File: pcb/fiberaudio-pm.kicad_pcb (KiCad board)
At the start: 2 copper layers, 25.4 x 22.9 mm, 9 parts, among them J1 Conn_01x06, J2 PLT237/T10WH, J3 PLR237/T10BK

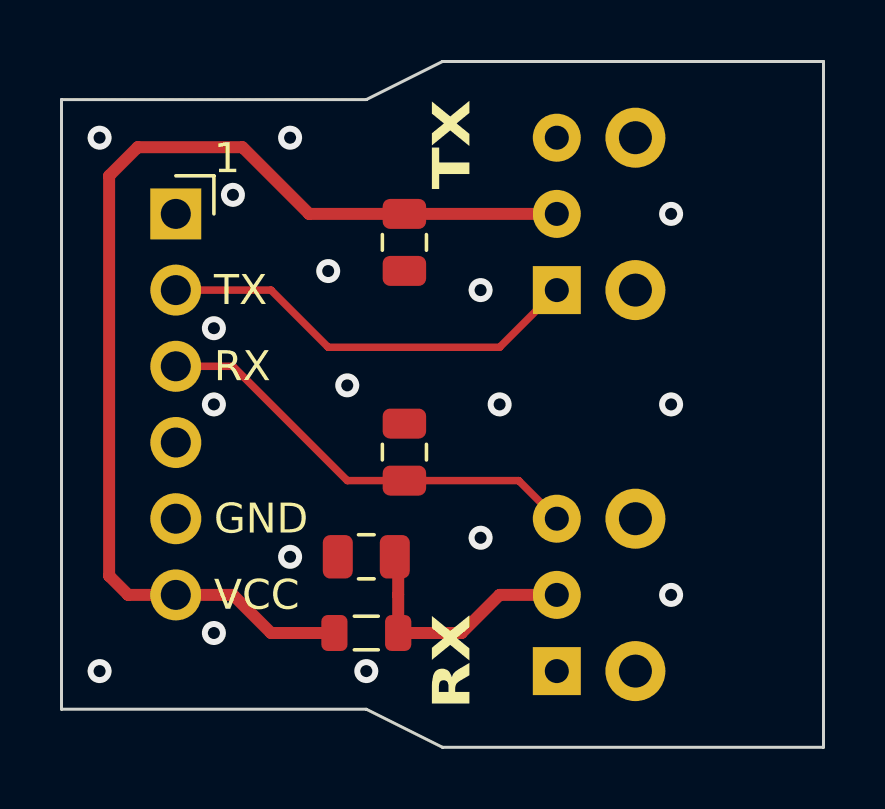
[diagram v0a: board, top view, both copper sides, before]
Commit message: Fixed pin-swap on J3; Updated to Rev.2; Updated documentation
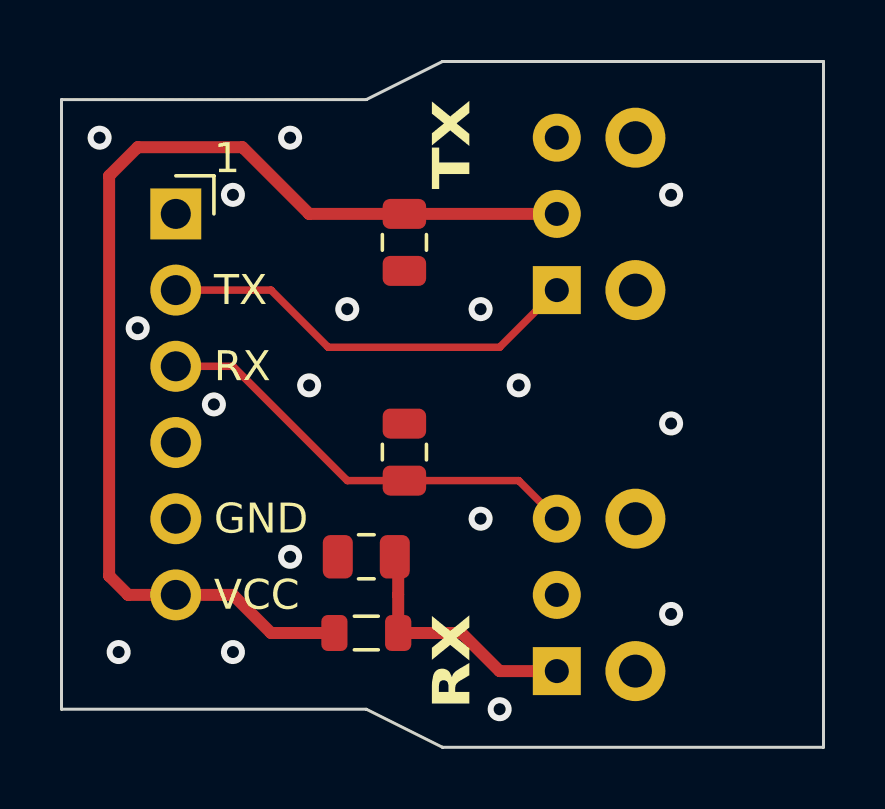
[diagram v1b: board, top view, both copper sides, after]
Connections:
- C31 pad 1: Net-(J3-VCC) -> Net-(J3-GND)
- J3 pad 1: GND -> Net-(J3-GND)
- J3 pad 2: Net-(J3-VCC) -> GND
- L31 pad 2: Net-(J3-VCC) -> Net-(J3-GND)
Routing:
- net Net-(J3-VCC): track 8.40 -> 0.00 mm
- net Net-(J3-GND): track 0.00 -> 8.40 mm
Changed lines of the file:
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@@
     (title "fiberaudio-pm")
     (date "2024-01-22")
-    (rev "1")
+    (rev "2")
     (company "https://github.com/islandcontroller/fiberaudio-pm")
   )
@@
   (net 0 "")
   (net 1 "GND")
-  (net 2 "Net-(J3-VCC)")
+  (net 2 "Net-(J3-GND)")
   (net 3 "/RX")
   (net 4 "unconnected-(J1-Pin_1-Pad1)")
@@
       (stroke (width 0.1) (type solid)) (layer "F.Fab"))
     (pad "1" smd roundrect (at -0.95 0 180) (size 1 1.45) (layers "F.Cu" "F.Paste" "F.Mask") (roundrect_rratio 0.25)
-      (net 2 "Net-(J3-VCC)") (pintype "passive"))
+      (net 2 "Net-(J3-GND)") (pintype "passive"))
     (pad "2" smd roundrect (at 0.95 0 180) (size 1 1.45) (layers "F.Cu" "F.Paste" "F.Mask") (roundrect_rratio 0.25)
       (net 1 "GND") (pintype "passive"))
@@
       (stroke (width 0.12) (type solid)) (layer "F.Fab"))
     (pad "1" thru_hole rect (at -2.54 0 90) (size 1.6 1.6) (drill 0.8) (layers "*.Cu" "*.Mask")
+      (net 2 "Net-(J3-GND)") (pinfunction "VCC") (pintype "power_in"))
+    (pad "2" thru_hole circle (at 0 0 90) (size 1.6 1.6) (drill 0.8) (layers "*.Cu" "*.Mask")
       (net 1 "GND") (pinfunction "GND") (pintype "power_in"))
-    (pad "2" thru_hole circle (at 0 0 90) (size 1.6 1.6) (drill 0.8) (layers "*.Cu" "*.Mask")
-      (net 2 "Net-(J3-VCC)") (pinfunction "VCC") (pintype "power_in"))
     (pad "3" thru_hole circle (at 2.54 0 90) (size 1.6 1.6) (drill 0.8) (layers "*.Cu" "*.Mask")
       (net 3 "/RX") (pinfunction "OUT") (pintype "output"))
@@
       (net 7 "VCC") (pinfunction "1") (pintype "passive"))
     (pad "2" smd roundrect (at 1.0625 0) (size 0.875 1.2) (layers "F.Cu" "F.Paste" "F.Mask") (roundrect_rratio 0.25)
-      (net 2 "Net-(J3-VCC)") (pinfunction "2") (pintype "passive"))
+      (net 2 "Net-(J3-GND)") (pinfunction "2") (pintype "passive"))
     (model "${KICAD6_3DMODEL_DIR}/Inductor_SMD.3dshapes/L_0805_2012Metric.wrl"
       (offset (xyz 0 0 0))
@@
     (effects (font (size 1.25 1.5) (thickness 0.25) bold) (justify right))
   )
-  (via (at 99.695 60.325) (size 0.8) (drill 0.4) (layers "F.Cu" "B.Cu") (free) (net 1))
+  (via (at 98.425 60.325) (size 0.8) (drill 0.4) (layers "F.Cu" "B.Cu") (free) (net 1))
   (via (at 97.79 66.04) (size 0.8) (drill 0.4) (layers "F.Cu" "B.Cu") (free) (net 1))
-  (via (at 104.775 60.96) (size 0.8) (drill 0.4) (layers "F.Cu" "B.Cu") (free) (net 1))
+  (via (at 105.41 60.325) (size 0.8) (drill 0.4) (layers "F.Cu" "B.Cu") (free) (net 1))
   (via (at 95.885 53.975) (size 0.8) (drill 0.4) (layers "F.Cu" "B.Cu") (free) (net 1))
-  (via (at 91.44 69.85) (size 0.8) (drill 0.4) (layers "F.Cu" "B.Cu") (free) (net 1))
-  (via (at 100.33 69.85) (size 0.8) (drill 0.4) (layers "F.Cu" "B.Cu") (free) (net 1))
-  (via (at 104.14 57.15) (size 0.8) (drill 0.4) (layers "F.Cu" "B.Cu") (free) (net 1))
-  (via (at 95.25 58.42) (size 0.8) (drill 0.4) (layers "F.Cu" "B.Cu") (free) (net 1))
-  (via (at 95.25 68.58) (size 0.8) (drill 0.4) (layers "F.Cu" "B.Cu") (free) (net 1))
-  (via (at 110.49 54.61) (size 0.8) (drill 0.4) (layers "F.Cu" "B.Cu") (free) (net 1))
-  (via (at 99.06 56.515) (size 0.8) (drill 0.4) (layers "F.Cu" "B.Cu") (free) (net 1))
-  (via (at 110.49 60.96) (size 0.8) (drill 0.4) (layers "F.Cu" "B.Cu") (free) (net 1))
-  (via (at 110.49 67.31) (size 0.8) (drill 0.4) (layers "F.Cu" "B.Cu") (free) (net 1))
-  (via (at 104.14 65.405) (size 0.8) (drill 0.4) (layers "F.Cu" "B.Cu") (free) (net 1))
+  (via (at 104.14 64.77) (size 0.8) (drill 0.4) (layers "F.Cu" "B.Cu") (free) (net 1))
+  (via (at 92.075 69.215) (size 0.8) (drill 0.4) (layers "F.Cu" "B.Cu") (free) (net 1))
+  (via (at 104.775 71.12) (size 0.8) (drill 0.4) (layers "F.Cu" "B.Cu") (free) (net 1))
+  (via (at 104.14 57.785) (size 0.8) (drill 0.4) (layers "F.Cu" "B.Cu") (free) (net 1))
+  (via (at 92.71 58.42) (size 0.8) (drill 0.4) (layers "F.Cu" "B.Cu") (free) (net 1))
+  (via (at 95.885 69.215) (size 0.8) (drill 0.4) (layers "F.Cu" "B.Cu") (free) (net 1))
+  (via (at 110.49 53.975) (size 0.8) (drill 0.4) (layers "F.Cu" "B.Cu") (free) (net 1))
+  (via (at 99.695 57.785) (size 0.8) (drill 0.4) (layers "F.Cu" "B.Cu") (free) (net 1))
+  (via (at 110.49 61.595) (size 0.8) (drill 0.4) (layers "F.Cu" "B.Cu") (free) (net 1))
+  (via (at 110.49 67.945) (size 0.8) (drill 0.4) (layers "F.Cu" "B.Cu") (free) (net 1))
   (via (at 95.25 60.96) (size 0.8) (drill 0.4) (layers "F.Cu" "B.Cu") (free) (net 1))
   (via (at 97.79 52.07) (size 0.8) (drill 0.4) (layers "F.Cu" "B.Cu") (free) (net 1))
   (via (at 91.44 52.07) (size 0.8) (drill 0.4) (layers "F.Cu" "B.Cu") (free) (net 1))
-  (segment (start 103.505 68.58) (end 101.3925 68.58) (width 0.4) (layer "F.Cu") (net 2))
-  (segment (start 106.68 67.31) (end 104.775 67.31) (width 0.4) (layer "F.Cu") (net 2))
-  (segment (start 104.775 67.31) (end 103.505 68.58) (width 0.4) (layer "F.Cu") (net 2))
+  (segment (start 101.3925 68.58) (end 103.505 68.58) (width 0.4) (layer "F.Cu") (net 2))
+  (segment (start 104.775 69.85) (end 106.68 69.85) (width 0.4) (layer "F.Cu") (net 2))
+  (segment (start 103.505 68.58) (end 104.775 69.85) (width 0.4) (layer "F.Cu") (net 2))
   (segment (start 101.3925 68.58) (end 101.3925 67.31) (width 0.4) (layer "F.Cu") (net 2))
   (segment (start 101.3925 66.1525) (end 101.28 66.04) (width 0.4) (layer "F.Cu") (net 2))

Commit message: Re-classified as 'component' acc. to FAQ on Directive 2012/19/EU (WEEE2), see http://ec.europa.eu/environment/waste/weee/pdf/faq.pdf; Removed WEEE logo; Added note regarding RoHS compliance requirement
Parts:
- removed the REF** at (100.3, 54.6)
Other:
- board text added: "Subject to compliance with RoHS Directive (EU) 2015/863 amending Annex II to Directive 2011/65/EU."

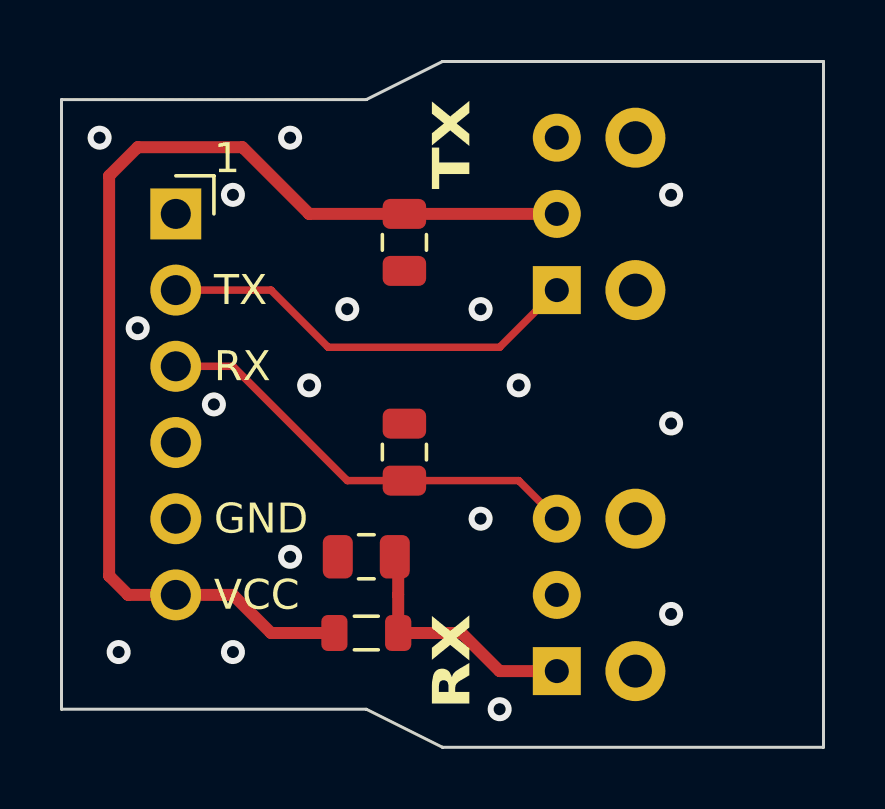
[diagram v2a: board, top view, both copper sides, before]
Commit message: Reduced thermal spoke width to 0.25um; Adjusted layout; Adjusted text placement and size
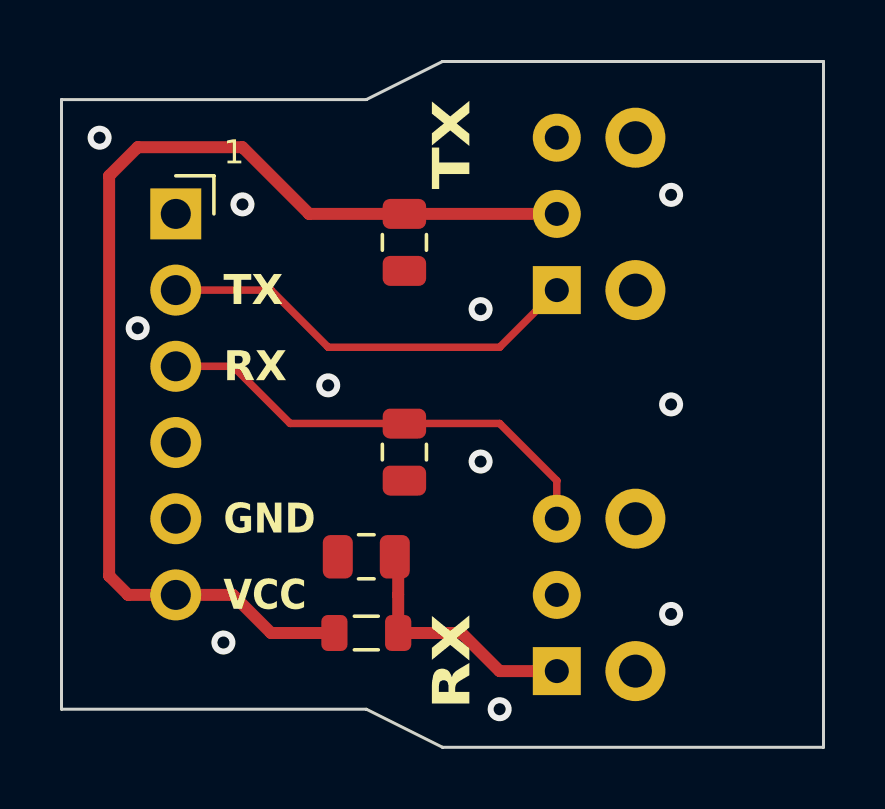
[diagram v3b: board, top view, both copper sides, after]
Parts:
- turned C32 to -90 degrees
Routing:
- net /RX: track 14.8 -> 15.5 mm
- net GND: vias 17 -> 11
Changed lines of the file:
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@@
   (title_block
     (title "fiberaudio-pm")
-    (date "2024-01-25")
-    (rev "3")
+    (date "2024-01-26")
+    (rev "4")
     (company "https://github.com/islandcontroller/fiberaudio-pm")
   )
@@
   (net 11 "unconnected-(J3-NC-Pad5)")
   (footprint "Capacitor_SMD:C_0805_2012Metric" (layer "F.Cu")
-    (at 101.6 62.55 90)
+    (at 101.6 62.55 -90)
     (descr "Capacitor SMD 0805 (2012 Metric), square (rectangular) end terminal, IPC_7351 nominal, (Body size source: IPC-SM-782 page 76, https://www.pcb-3d.com/wordpress/wp-content/uploads/ipc-sm-782a_amendment_1_and_2.pdf, https://docs.google.com/spreadsheets/d/1BsfQQcO9C6DZCsRaXUlFlo91Tg2WpOkGARC1WS5S8t0/edit?usp=sharing), generated with kicad-footprint-generator")
     (tags "capacitor")
@@
     (fp_line (start 1 0.625) (end -1 0.625)
       (stroke (width 0.1) (type solid)) (layer "F.Fab"))
-    (pad "1" smd roundrect (at -0.95 0 90) (size 1 1.45) (layers "F.Cu" "F.Paste" "F.Mask") (roundrect_rratio 0.25)
+    (pad "1" smd roundrect (at -0.95 0 270) (size 1 1.45) (layers "F.Cu" "F.Paste" "F.Mask") (roundrect_rratio 0.25)
       (net 3 "/RX") (pintype "passive"))
-    (pad "2" smd roundrect (at 0.95 0 90) (size 1 1.45) (layers "F.Cu" "F.Paste" "F.Mask") (roundrect_rratio 0.25)
+    (pad "2" smd roundrect (at 0.95 0 270) (size 1 1.45) (layers "F.Cu" "F.Paste" "F.Mask") (roundrect_rratio 0.25)
       (net 1 "GND") (pintype "passive"))
     (model "${KICAD6_3DMODEL_DIR}/Capacitor_SMD.3dshapes/C_0805_2012Metric.wrl"
@@
     (pad "4" thru_hole oval (at 0 7.62) (size 1.7 1.7) (drill 1) (layers "*.Cu" "*.Mask")
       (net 6 "unconnected-(J1-Pin_4-Pad4)") (pinfunction "Pin_4") (pintype "passive+no_connect"))
-    (pad "5" thru_hole oval (at 0 10.16) (size 1.7 1.7) (drill 1) (layers "*.Cu" "*.Mask")
+    (pad "5" thru_hole oval (at 0 10.16 45) (size 1.7 1.7) (drill 1) (layers "*.Cu" "*.Mask")
       (net 1 "GND") (pinfunction "Pin_5") (pintype "passive"))
     (pad "6" thru_hole oval (at 0 12.7) (size 1.7 1.7) (drill 1) (layers "*.Cu" "*.Mask")
@@
     (effects (font (size 1.25 1.5) (thickness 0.25) bold) (justify left))
   )
-  (gr_text "TX" (at 95.25 57.15) (layer "F.SilkS")
-    (effects (font (size 1 1) (thickness 0.15)) (justify left))
-  )
-  (gr_text "GND" (at 95.25 64.77) (layer "F.SilkS")
-    (effects (font (size 1 1) (thickness 0.15)) (justify left))
-  )
-  (gr_text "1" (at 95.25 53.34) (layer "F.SilkS")
-    (effects (font (size 1 1) (thickness 0.15)) (justify left bottom))
-  )
-  (gr_text "RX" (at 95.25 59.69) (layer "F.SilkS")
-    (effects (font (size 1 1) (thickness 0.15)) (justify left))
-  )
-  (gr_text "VCC" (at 95.25 67.31) (layer "F.SilkS")
-    (effects (font (size 1 1) (thickness 0.15)) (justify left))
+  (gr_text "TX" (at 95.5675 57.15) (layer "F.SilkS")
+    (effects (font (size 1 1) (thickness 0.2) bold) (justify left))
+  )
+  (gr_text "GND" (at 95.5675 64.77) (layer "F.SilkS")
+    (effects (font (size 1 0.9) (thickness 0.2) bold) (justify left))
+  )
+  (gr_text "1" (at 95.5675 53.0225) (layer "F.SilkS")
+    (effects (font (size 0.8 0.8) (thickness 0.15)) (justify left bottom))
+  )
+  (gr_text "RX" (at 95.5675 59.69) (layer "F.SilkS")
+    (effects (font (size 1 1) (thickness 0.2) bold) (justify left))
+  )
+  (gr_text "VCC" (at 95.5675 67.31) (layer "F.SilkS")
+    (effects (font (size 1 0.9) (thickness 0.2) bold) (justify left))
   )
   (gr_text "TX" (at 103.1875 50.8 90) (layer "F.SilkS")
@@
     (effects (font (size 1 1) (thickness 0.15)) (justify left top))
   )
-  (via (at 98.425 60.325) (size 0.8) (drill 0.4) (layers "F.Cu" "B.Cu") (free) (net 1))
-  (via (at 97.79 66.04) (size 0.8) (drill 0.4) (layers "F.Cu" "B.Cu") (free) (net 1))
-  (via (at 105.41 60.325) (size 0.8) (drill 0.4) (layers "F.Cu" "B.Cu") (free) (net 1))
-  (via (at 95.885 53.975) (size 0.8) (drill 0.4) (layers "F.Cu" "B.Cu") (free) (net 1))
-  (via (at 104.14 64.77) (size 0.8) (drill 0.4) (layers "F.Cu" "B.Cu") (free) (net 1))
-  (via (at 92.075 69.215) (size 0.8) (drill 0.4) (layers "F.Cu" "B.Cu") (free) (net 1))
+  (via (at 96.2025 54.2925) (size 0.8) (drill 0.4) (layers "F.Cu" "B.Cu") (free) (net 1))
+  (via (at 104.14 62.865) (size 0.8) (drill 0.4) (layers "F.Cu" "B.Cu") (free) (net 1))
+  (via (at 95.5675 68.8975) (size 0.8) (drill 0.4) (layers "F.Cu" "B.Cu") (free) (net 1))
   (via (at 104.775 71.12) (size 0.8) (drill 0.4) (layers "F.Cu" "B.Cu") (free) (net 1))
   (via (at 104.14 57.785) (size 0.8) (drill 0.4) (layers "F.Cu" "B.Cu") (free) (net 1))
   (via (at 92.71 58.42) (size 0.8) (drill 0.4) (layers "F.Cu" "B.Cu") (free) (net 1))
-  (via (at 95.885 69.215) (size 0.8) (drill 0.4) (layers "F.Cu" "B.Cu") (free) (net 1))
   (via (at 110.49 53.975) (size 0.8) (drill 0.4) (layers "F.Cu" "B.Cu") (free) (net 1))
-  (via (at 99.695 57.785) (size 0.8) (drill 0.4) (layers "F.Cu" "B.Cu") (free) (net 1))
-  (via (at 110.49 61.595) (size 0.8) (drill 0.4) (layers "F.Cu" "B.Cu") (free) (net 1))
+  (via (at 110.49 60.96) (size 0.8) (drill 0.4) (layers "F.Cu" "B.Cu") (free) (net 1))
   (via (at 110.49 67.945) (size 0.8) (drill 0.4) (layers "F.Cu" "B.Cu") (free) (net 1))
-  (via (at 95.25 60.96) (size 0.8) (drill 0.4) (layers "F.Cu" "B.Cu") (free) (net 1))
-  (via (at 97.79 52.07) (size 0.8) (drill 0.4) (layers "F.Cu" "B.Cu") (free) (net 1))
+  (via (at 99.06 60.325) (size 0.8) (drill 0.4) (layers "F.Cu" "B.Cu") (free) (net 1))
   (via (at 91.44 52.07) (size 0.8) (drill 0.4) (layers "F.Cu" "B.Cu") (free) (net 1))
   (segment (start 101.3925 68.58) (end 103.505 68.58) (width 0.4) (layer "F.Cu") (net 2))
@@
   (segment (start 101.3925 66.1525) (end 101.28 66.04) (width 0.4) (layer "F.Cu") (net 2))
   (segment (start 101.3925 67.31) (end 101.3925 66.1525) (width 0.4) (layer "F.Cu") (net 2))
-  (segment (start 99.695 63.5) (end 101.6 63.5) (width 0.25) (layer "F.Cu") (net 3))
-  (segment (start 105.41 63.5) (end 106.68 64.77) (width 0.25) (layer "F.Cu") (net 3))
-  (segment (start 95.885 59.69) (end 99.695 63.5) (width 0.25) (layer "F.Cu") (net 3))
-  (segment (start 101.6 63.5) (end 105.41 63.5) (width 0.25) (layer "F.Cu") (net 3))
+  (segment (start 104.775 61.595) (end 106.68 63.5) (width 0.25) (layer "F.Cu") (net 3))
+  (segment (start 106.68 63.5) (end 106.68 64.77) (width 0.25) (layer "F.Cu") (net 3))
+  (segment (start 97.79 61.595) (end 104.775 61.595) (width 0.25) (layer "F.Cu") (net 3))
   (segment (start 93.98 59.69) (end 95.885 59.69) (width 0.25) (layer "F.Cu") (net 3))
+  (segment (start 95.885 59.69) (end 97.79 61.595) (width 0.25) (layer "F.Cu") (net 3))
   (segment (start 93.98 57.15) (end 97.155 57.15) (width 0.25) (layer "F.Cu") (net 5))
   (segment (start 99.06 59.055) (end 104.775 59.055) (width 0.25) (layer "F.Cu") (net 5))
@@
     (polygon
       (pts
-        (xy 99.232867 67.705525)
-        (xy 101.307686 67.721862)
-        (xy 101.307686 69.40459)
-        (xy 99.200192 69.388253)
+        (xy 99.06 67.945)
+        (xy 101.307686 67.945)
+        (xy 101.307686 69.215)
+        (xy 99.06 69.215)
       )
     )
@@
     (connect_pads (clearance 0.25))
     (min_thickness 0.25) (filled_areas_thickness no)
-    (fill yes (thermal_gap 0.25) (thermal_bridge_width 0.508))
+    (fill yes (thermal_gap 0.25) (thermal_bridge_width 0.25))
     (polygon
       (pts
@@
     (connect_pads (clearance 0.25))
     (min_thickness 0.25) (filled_areas_thickness no)
-    (fill yes (thermal_gap 0.25) (thermal_bridge_width 0.508))
+    (fill yes (thermal_gap 0.25) (thermal_bridge_width 0.25))
     (polygon
       (pts
